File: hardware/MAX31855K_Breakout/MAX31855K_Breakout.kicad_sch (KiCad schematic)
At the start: 16 parts, among them J1 Conn_01x02_Socket, J2 Conn_01x02_Socket, J3 Conn_01x03_Socket, U1 MAX31855KASA, U2 TPS631000

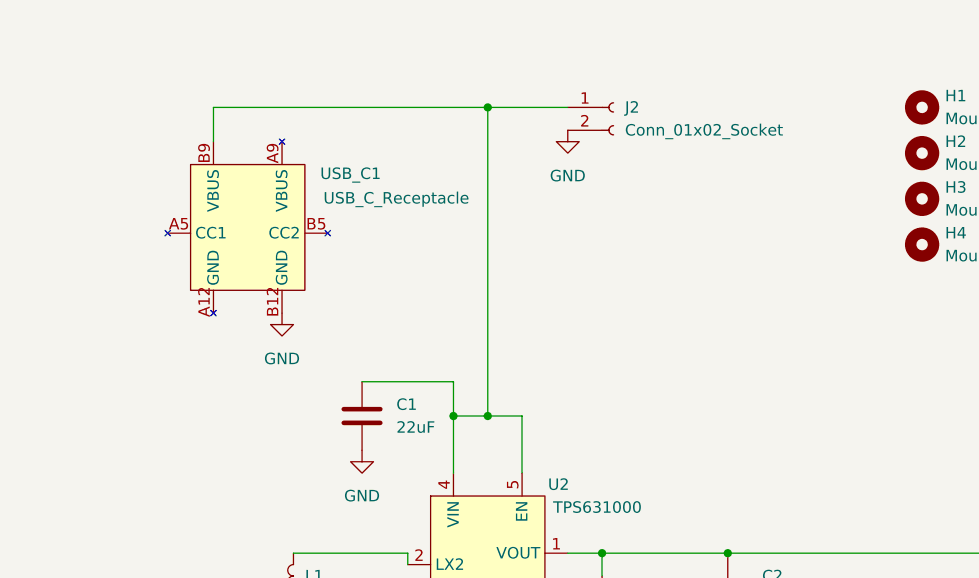
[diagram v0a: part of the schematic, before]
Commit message: fix: add 5.1k resistors to USB-C CC pins (#5)
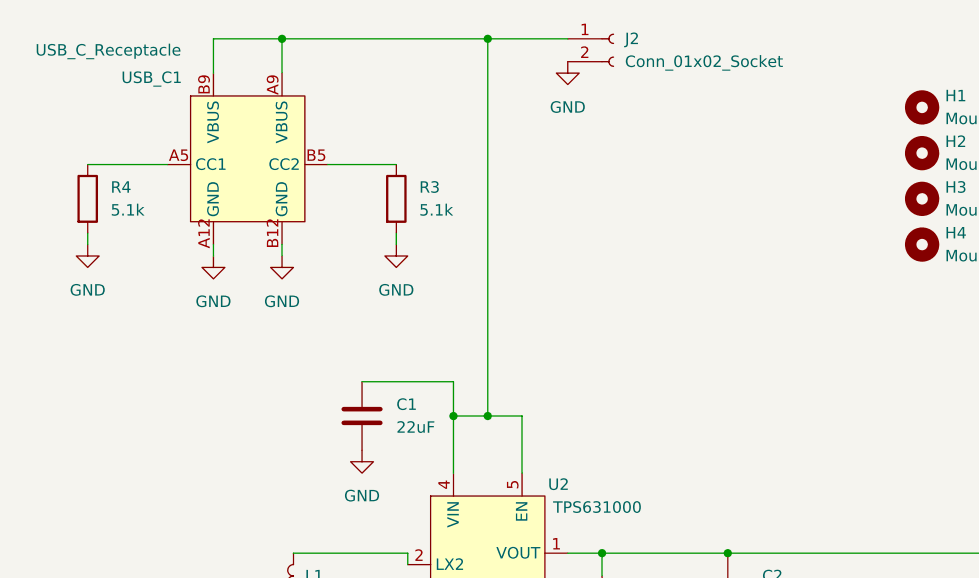
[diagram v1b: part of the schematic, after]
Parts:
- added R3, R4: 5.1k, Resistor_SMD:R_0805_2012Metric, symbol Device:R
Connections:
- net GND: now also USB_C1.A12 (GND), R3.2, R4.2
- net at C1.1, J2.1 (Pin_1), U2.4 (VIN)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: now also USB_C1.A9 (VBUS)
- net at USB_C1.A5 (CC1): now also R4.1
- net at USB_C1.B5 (CC2): now also R3.1
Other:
- moved on the sheet: J2

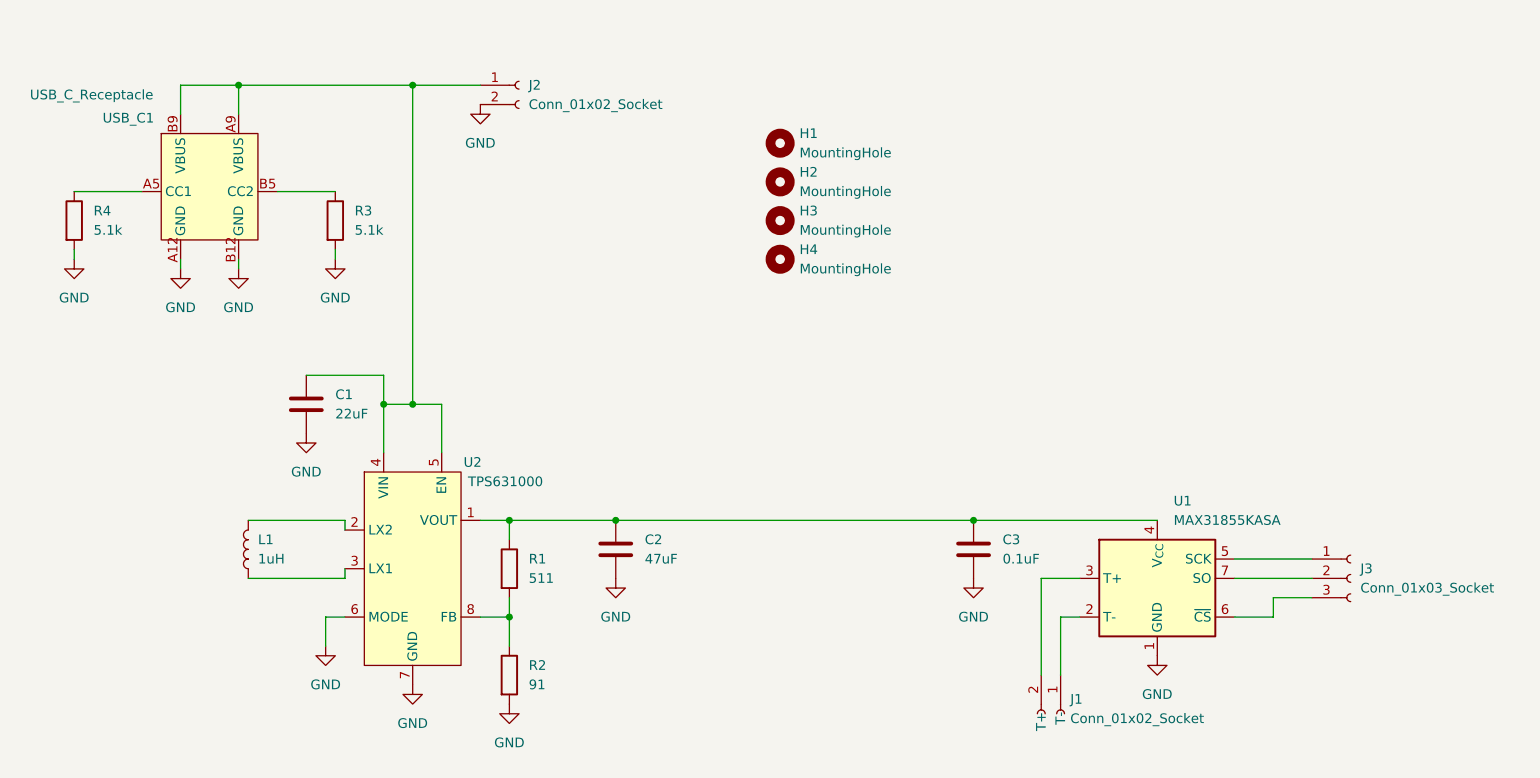
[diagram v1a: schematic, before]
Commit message: feat: add mosfet to board for signal (#8)
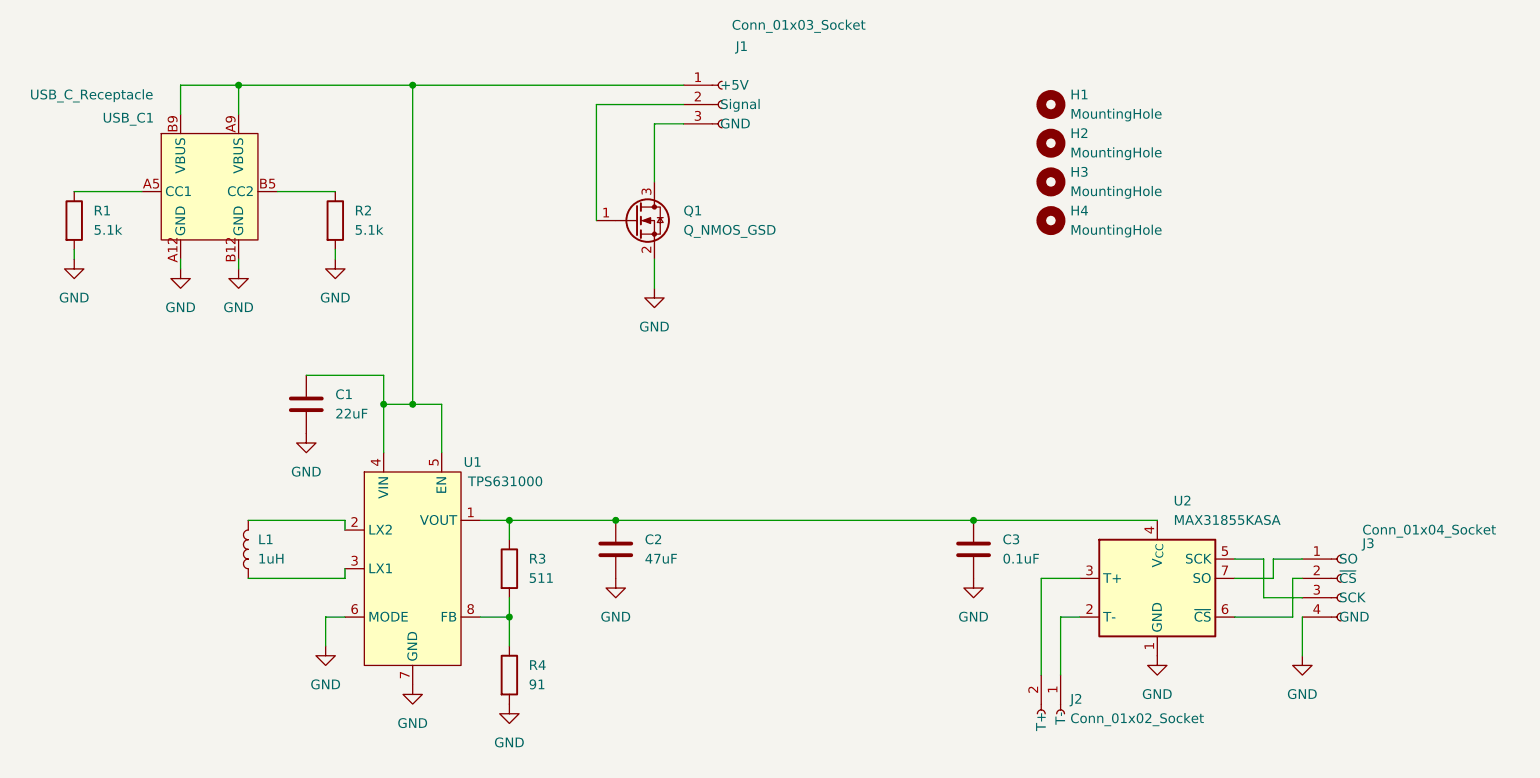
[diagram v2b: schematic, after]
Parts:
- removed J2: Conn_01x02_Socket, Connector_JST:JST_XH_B2B-XH-A_1x02_P2.50mm_Vertical, symbol Connector:Conn_01x02_Socket
- removed J3: Conn_01x03_Socket, Connector_JST:JST_XH_B3B-XH-A_1x03_P2.50mm_Vertical, symbol Connector:Conn_01x03_Socket
- added J1: Conn_01x03_Socket, Connector_JST:JST_XH_B3B-XH-A_1x03_P2.50mm_Vertical, symbol Connector:Conn_01x03_Socket
- added J3: Conn_01x04_Socket, Connector_JST:JST_XH_B4B-XH-A_1x04_P2.50mm_Vertical, symbol Connector:Conn_01x04_Socket
- added Q1: Q_NMOS_GSD, Package_TO_SOT_SMD:SOT-23-3, symbol Transistor_FET:Q_NMOS_GSD
- C1: DigiKey Part Number (none) -> 490-GRM21BZ71A226ME15LCT-ND
- C2: DigiKey Part Number (none) -> 490-9961-1-ND
- C3: DigiKey Part Number (none) -> 311-1140-1-ND
- J2: renamed from J1; DigiKey Part Number (none) -> 455-B2B-XH-A-ND
- L1: DigiKey Part Number (none) -> 541-IHHP0805ZHER1R0M01CT-ND
- R1: renamed from R4; DigiKey Part Number (none) -> 311-5.1KARCT-ND
- R2: renamed from R3; DigiKey Part Number (none) -> 311-5.1KARCT-ND
- R3: renamed from R1; DigiKey Part Number (none) -> 311-511CRCT-ND
- R4: renamed from R2; DigiKey Part Number (none) -> P91.0CCT-ND
- U1: renamed from U2; DigiKey Part Number (none) -> 296-TPS631000DRLRCT-ND
- U2: renamed from U1; DigiKey Part Number (none) -> MAX31855KASA+TCT-ND
- USB_C1: DigiKey Part Number (none) -> 900-2171750001CT-ND
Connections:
- net GND: now also J3.4 (GND), Q1.2 (S)
- net at U2.5 (SCK): now also J3.3 (SCK)
- net at U2.6 (~{CS}): now also J3.2 (~{CS})
- net at U2.7 (SO): now also J3.1 (SO)
- net at C1.1, U1.4 (VIN), U1.5 (EN)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: now also J1.1 (+5V)
- new net: J1.2 (Signal), Q1.1 (G)
- new net: J1.3 (GND), Q1.3 (D)
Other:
- moved on the sheet: H1, H2, H3, H4

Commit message: fix: fix parity (#10)
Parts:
- renumbered J2 to J1, J1 to J2, R3 to R1, R4 to R2, R2 to R3, R1 to R4, U2 to U1, U1 to U2
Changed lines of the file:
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@@
 		(dnp no)
 		(fields_autoplaced yes)
-		(property "Reference" "J2"
+		(property "Reference" "J1"
 			(at 186.69 121.2849 90)
 			(effects
@@
 			(project ""
 				(path "/a793c5ac-b66c-4259-9d59-43bd772bada2"
-					(reference "J2")
+					(reference "J1")
 					(unit 1)
 				)
@@
 		(dnp no)
 		(fields_autoplaced yes)
-		(property "Reference" "U2"
+		(property "Reference" "U1"
 			(at 200.2633 95.25 0)
 			(effects
@@
 			(project ""
 				(path "/a793c5ac-b66c-4259-9d59-43bd772bada2"
-					(reference "U2")
+					(reference "U1")
 					(unit 1)
 				)
@@
 		(dnp no)
 		(fields_autoplaced yes)
-		(property "Reference" "R2"
+		(property "Reference" "R3"
 			(at 92.71 57.1499 0)
 			(effects
@@
 			(project ""
 				(path "/a793c5ac-b66c-4259-9d59-43bd772bada2"
-					(reference "R2")
+					(reference "R3")
 					(unit 1)
 				)
@@
 		(on_board yes)
 		(dnp no)
-		(property "Reference" "J1"
+		(property "Reference" "J2"
 			(at 142.748 35.56 0)
 			(effects
@@
 			(project ""
 				(path "/a793c5ac-b66c-4259-9d59-43bd772bada2"
-					(reference "J1")
+					(reference "J2")
 					(unit 1)
 				)
@@
 		(dnp no)
 		(fields_autoplaced yes)
-		(property "Reference" "R4"
+		(property "Reference" "R2"
 			(at 115.57 116.8399 0)
 			(effects
@@
 			(project "MAX31855K_Breakout"
 				(path "/a793c5ac-b66c-4259-9d59-43bd772bada2"
-					(reference "R4")
+					(reference "R2")
 					(unit 1)
 				)
@@
 		(on_board yes)
 		(dnp no)
-		(property "Reference" "U1"
+		(property "Reference" "U2"
 			(at 108.204 90.17 0)
 			(effects
@@
 			(project ""
 				(path "/a793c5ac-b66c-4259-9d59-43bd772bada2"
-					(reference "U1")
+					(reference "U2")
 					(unit 1)
 				)
@@
 		(dnp no)
 		(fields_autoplaced yes)
-		(property "Reference" "R3"
+		(property "Reference" "R1"
 			(at 115.57 102.8699 0)
 			(effects
@@
 			(project ""
 				(path "/a793c5ac-b66c-4259-9d59-43bd772bada2"
-					(reference "R3")
+					(reference "R1")
 					(unit 1)
 				)
@@
 		(dnp no)
 		(fields_autoplaced yes)
-		(property "Reference" "R1"
+		(property "Reference" "R4"
 			(at 58.42 57.1499 0)
 			(effects
@@
 			(project "MAX31855K_Breakout"
 				(path "/a793c5ac-b66c-4259-9d59-43bd772bada2"
-					(reference "R1")
-					(unit 1)
-				)
+					(reference "R4")
+					(unit 1)
+				)

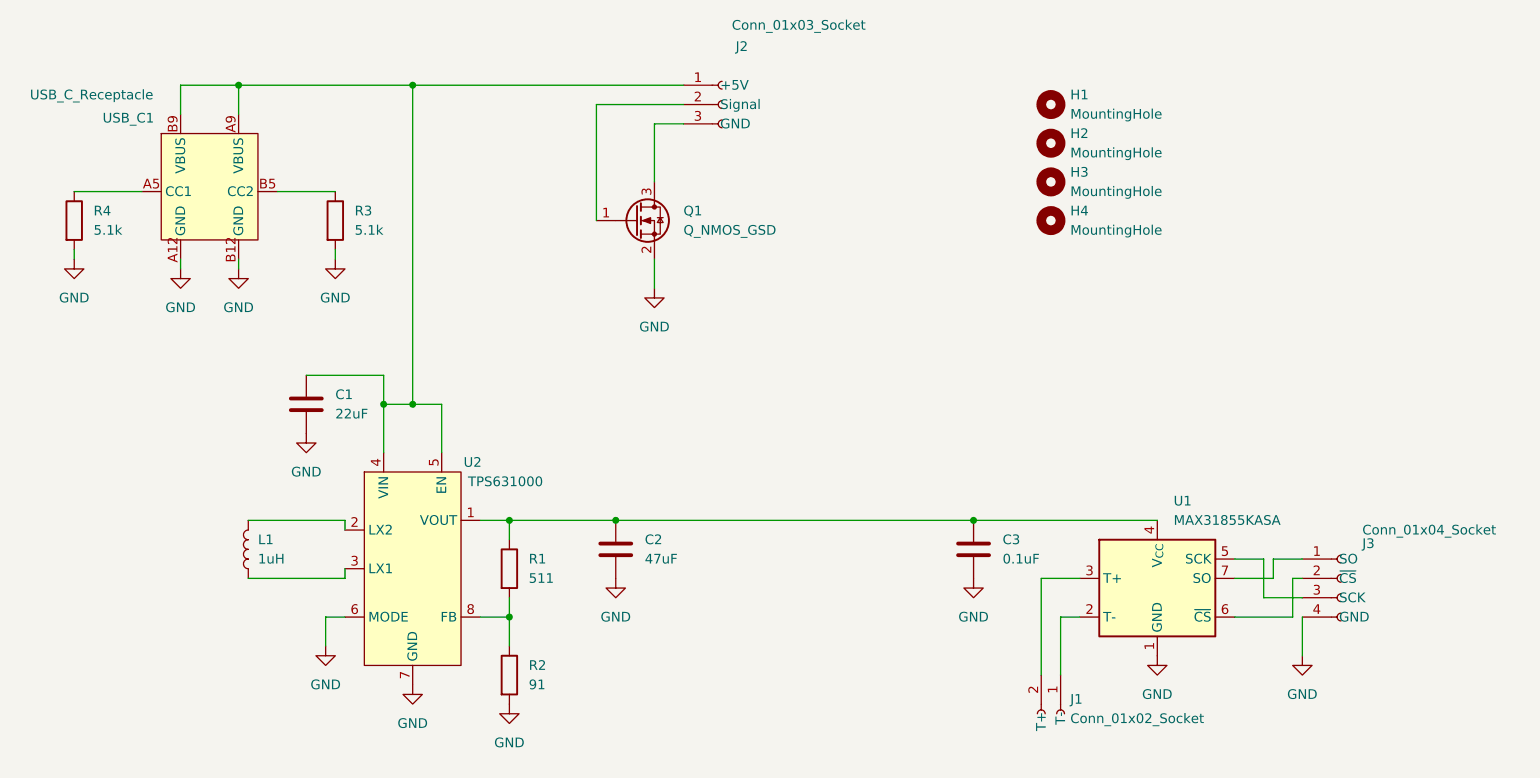
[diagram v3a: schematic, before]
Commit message: chore: add copy of temp. sensor with reorganized pins (#11)
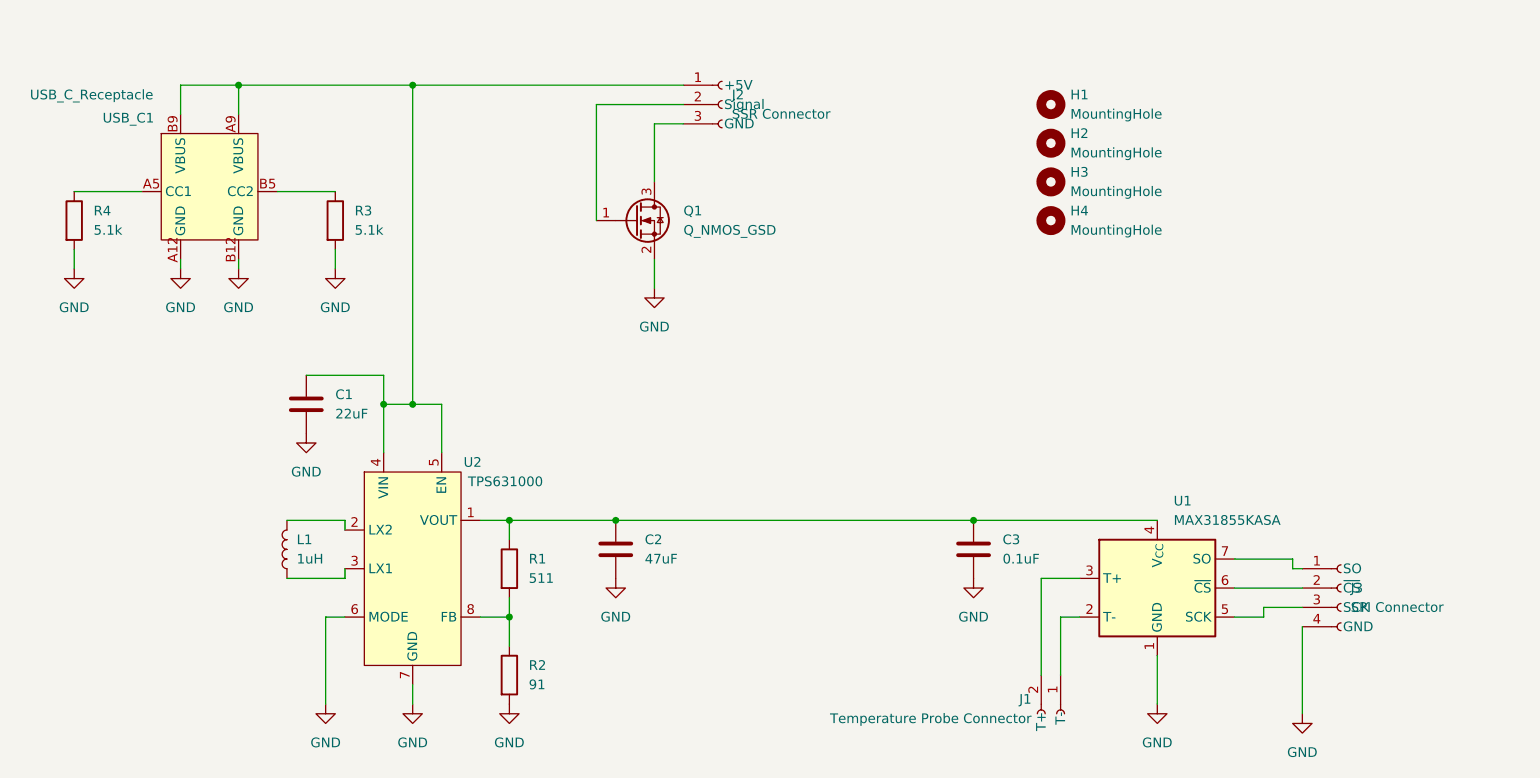
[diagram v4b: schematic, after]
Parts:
- removed J1: Conn_01x02_Socket, Connector_JST:JST_XH_B2B-XH-A_1x02_P2.50mm_Vertical, symbol Connector:Conn_01x02_Socket
- added J1: Temperature Probe Connector, Connector_JST:JST_XH_B2B-XH-A_1x02_P2.50mm_Vertical, symbol Reflow_Oven:Temperature Probe Connector
- J2: value Conn_01x03_Socket -> SSR Connector; symbol Connector:Conn_01x03_Socket -> Reflow_Oven:SSR Connector
- J3: value Conn_01x04_Socket -> SPI Connector; symbol Connector:Conn_01x04_Socket -> Reflow_Oven:SPI Connector
- U1: symbol Sensor_Temperature:MAX31855KASA -> Reflow_Oven:MAX31855KASA
- USB_C1: footprint User:USB_C_Receptacle -> Reflow_Oven:USB_C_Receptacle; symbol User:USB_C_Receptacle -> Reflow_Oven:USB_C_Receptacle
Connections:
- net at U1.2 (T-): now also J1.1 (T-)
- net at U1.3 (T+): now also J1.2 (T+)
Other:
- moved on the sheet: J3, L1

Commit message: --wip-- [skip ci]
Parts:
- U2: symbol User:TPS631000 -> Reflow_Oven:TPS631000; DigiKey Part Number 296-TPS631000DRLRCT-ND -> (none)
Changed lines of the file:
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@@
 		)
 		(property "DigiKey Part Number" "MAX31855KASA+TCT-ND"
-			(at 198.12 107.95 0)
+			(at 213.36 123.19 0)
 			(effects
 				(font
@@
 	)
 	(symbol
-		(lib_id "User:TPS631000")
+		(lib_id "Reflow_Oven:TPS631000")
 		(at 100.33 104.14 0)
 		(unit 1)
@@
 		(dnp no)
 		(property "Reference" "U2"
-			(at 108.204 90.17 0)
+			(at 100.33 104.14 0)
 			(effects
 				(font
@@
 		)
 		(property "Value" "TPS631000"
-			(at 112.522 92.71 0)
+			(at 86.36 115.57 0)
 			(effects
 				(font
@@
 			(effects
 				(font
-					(size 1.27 1.27)
-				)
-				(hide yes)
-			)
-		)
-		(property "DigiKey Part Number" "296-TPS631000DRLRCT-ND"
-			(at 100.33 104.14 0)
-			(effects
-				(font
